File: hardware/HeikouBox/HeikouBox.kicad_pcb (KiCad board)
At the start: 2 copper layers, 100 x 100 mm, 198 parts, among them J101 5V, J201 Conn_02x05_Odd_Even, J202 Conn_02x08_Odd_Even, J301 DB15_Female_HighDensity_Mount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, J302 AudioJack3_SwitchTR, J501 Micro_SD_Card_TFP09-2-12B, J503 PS/2, Q301 MMBT3904, Q302 MMBT3904, Q303 MMBT3904, Q304 MMBT3904, Q305 MMBT3904, Q306 MMBT3904, Q307 MMBT3904, Q502 BSS138, Q503 BSS138, SW501 Left, SW502 Right, SW503 Up, SW504 Down, U101 LD1117S33TR, U102 LD1117S25TR, U103 LD1117S12TR, U201 HeikouBox-Core, U202 74HCU04, U401 K4S281632-UC60, U501 STM32-BluePill-Socket, Y201 14.31818MHz, Y202 28.37516MHz

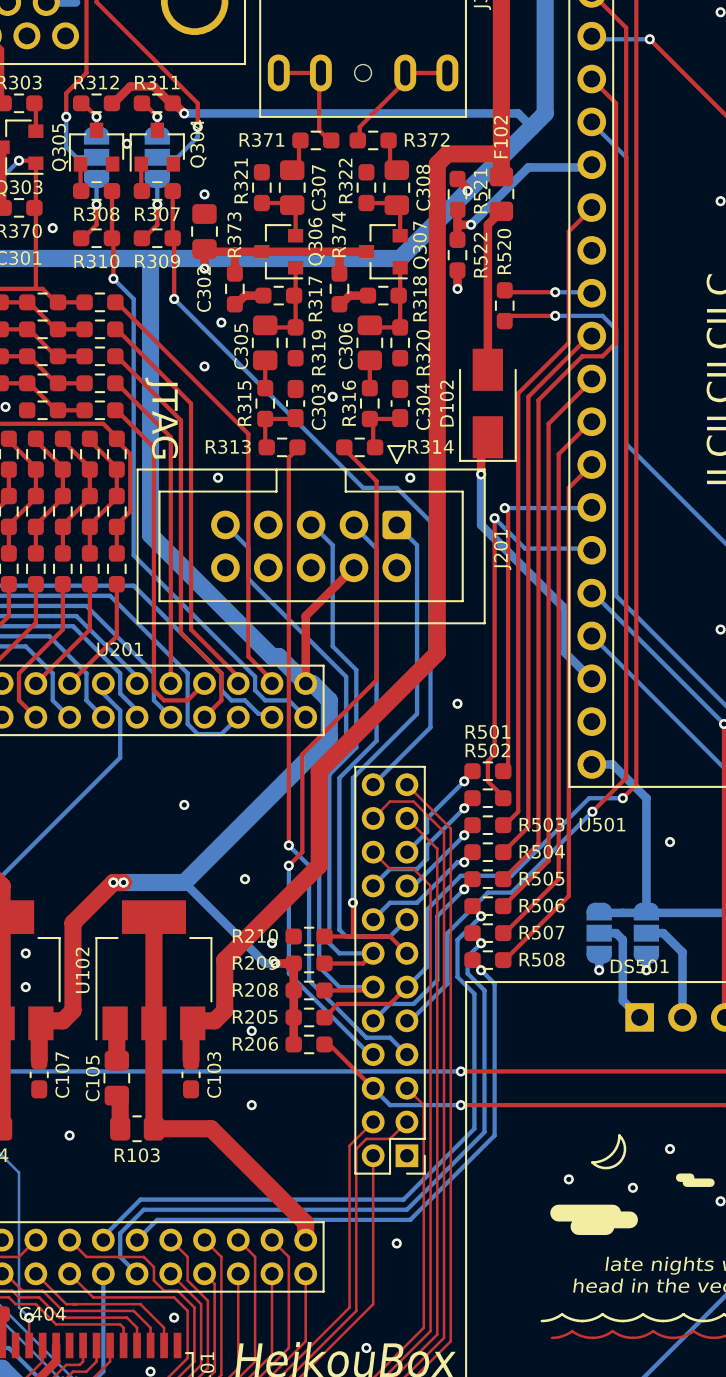
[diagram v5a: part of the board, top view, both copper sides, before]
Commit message: Connect UART correctly, remove unused mdb connection & mdb terminology
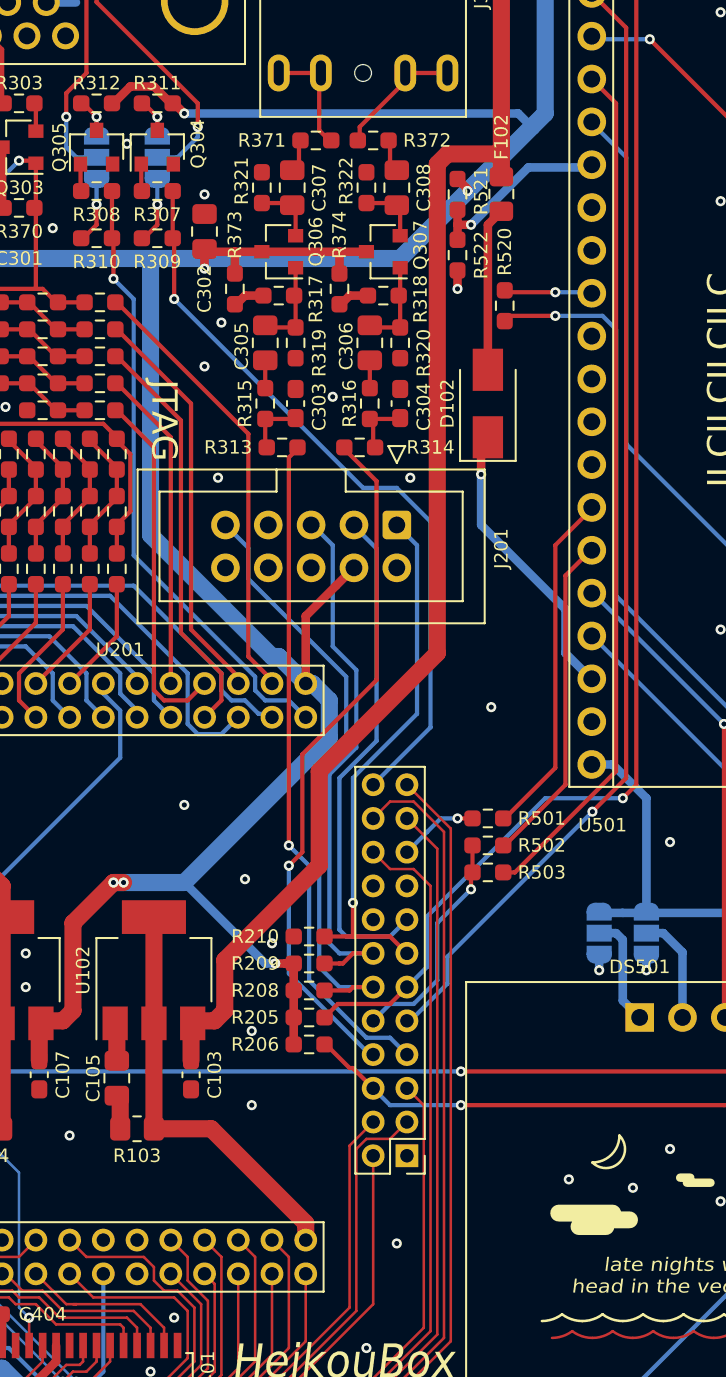
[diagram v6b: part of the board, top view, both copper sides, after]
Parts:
- removed R504, R505, R506, R507, R508: 1K, Resistor_SMD:R_0603_1608Metric_Pad0.98x0.95mm_HandSolder
- R313, R314: value 1K -> 2K2
- R315, R316: value 10K -> 1K
- moved R503 2.80 mm to (68.0, 77.4)
- moved R501 2.80 mm to (68.0, 74.2)
- moved R502 2.80 mm to (68.0, 75.8)
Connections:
- net /part2-core/mdb0 renamed /part2-core/dbg_RX
- net /part5-hub/MDB0_RX_R renamed /part5-hub/DBG_TX_R
- net /part5-hub/MDB1_TX_R renamed /part5-hub/DBG_RX_R
- D504 pad 2: Net-(D504-Pad2) -> (no net)
- J201 pad 6: Net-(J201-Pad6) -> (no net)
- J201 pad 7: Net-(J201-Pad7) -> (no net)
- J201 pad 8: Net-(J201-Pad8) -> (no net)
- J301 pad 11: Net-(J301-Pad11) -> (no net)
- J301 pad 12: Net-(J301-Pad12) -> (no net)
- J301 pad 15: Net-(J301-Pad15) -> (no net)
- J301 pad 4: Net-(J301-Pad4) -> (no net)
- J301 pad 5: Net-(J301-Pad5) -> (no net)
- J301 pad 9: Net-(J301-Pad9) -> (no net)
- J501 pad 1: Net-(J501-Pad1) -> (no net)
- J501 pad 8: Net-(J501-Pad8) -> (no net)
- J503 pad 2: Net-(J503-Pad2) -> (no net)
- J503 pad 6: Net-(J503-Pad6) -> (no net)
- R502 pad 2: /part2-core/mdb1 -> /part5-hub/cfg_DATA_dbg_RX
- R503 pad 1: /part5-hub/MDB2_R -> /part5-hub/CFG_DATA_R
- R503 pad 2: /part2-core/mdb2 -> /part5-hub/cfg_DATA_dbg_RX
- U201 pad 10: /part2-core/mdb4 -> /part5-hub/cfg_DATA_dbg_RX
- U201 pad 16: /part2-core/mdb3 -> (no net)
- U201 pad 17: /part2-core/mdb2 -> (no net)
- U201 pad 18: /part2-core/mdb1 -> (no net)
- U201 pad 83: /part2-core/mdb7 -> (no net)
- U201 pad 84: /part2-core/mdb6 -> (no net)
- U201 pad 85: /part2-core/mdb5 -> (no net)
- U202 pad 6: Net-(U202-Pad6) -> (no net)
- U202 pad 8: Net-(U202-Pad8) -> (no net)
- U401 pad 36: Net-(U401-Pad36) -> (no net)
- U401 pad 40: Net-(U401-Pad40) -> (no net)
- U501 pad 1: Net-(U501-Pad1) -> (no net)
- U501 pad 17: Net-(U501-Pad17) -> (no net)
- U501 pad 18: Net-(U501-Pad18) -> (no net)
- U501 pad 2: Net-(U501-Pad2) -> (no net)
- U501 pad 24: /part5-hub/MDB4_CD_R -> /part5-hub/CFG_DATA_R
- U501 pad 27: /part5-hub/MDB2_R -> (no net)
- U501 pad 28: Net-(U501-Pad28) -> (no net)
- U501 pad 3: Net-(U501-Pad3) -> (no net)
- U501 pad 30: /part5-hub/MDB3_R -> (no net)
- U501 pad 31: /part5-hub/MDB5_R -> (no net)
- U501 pad 32: /part5-hub/MDB6_R -> (no net)
- U501 pad 33: /part5-hub/MDB7_R -> (no net)
- U501 pad 4: Net-(U501-Pad4) -> (no net)
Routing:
- net /part5-hub/MDB4_CD_R: track 51.5 -> 0.00 mm
- net /part5-hub/CFG_DATA_R: track 0.00 -> 50.8 mm
- net /part2-core/mdb6: track 39.7 -> 0.00 mm, vias 1 -> 0
- net /part2-core/mdb5: track 39.3 -> 0.00 mm, vias 1 -> 0
- net /part5-hub/MDB2_R: track 38.8 -> 0.00 mm
- net /part2-core/mdb7: track 34.7 -> 0.00 mm, vias 1 -> 0
- net /part5-hub/MDB5_R: track 33.4 -> 0.00 mm
- net /part5-hub/MDB3_R: track 32.9 -> 0.00 mm
- net /part5-hub/MDB6_R: track 32.6 -> 0.00 mm
- net /part5-hub/MDB7_R: track 31.6 -> 0.00 mm
- net /part5-hub/cfg_DATA_dbg_RX: track 0.00 -> 13.7 mm, vias 0 -> 1
- net /part2-core/mdb4: track 11.7 -> 0.00 mm, vias 1 -> 0
- net /part2-core/mdb1: track 8.58 -> 0.00 mm, vias 1 -> 0
- net /part2-core/mdb3: track 7.61 -> 0.00 mm, vias 1 -> 0
- net /part2-core/mdb2: track 5.44 -> 0.00 mm, vias 1 -> 0
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
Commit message: Tidy PCB a bit
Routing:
- net /part2-core/jtag_TDO: track 30.0 -> 27.5 mm
- net /part2-core/cfg_NCFG: track 76.5 -> 74.8 mm
- net /part2-core/jtag_TDI: track 36.5 -> 35.3 mm
- net /part2-core/jtag_TMS: track 32.6 -> 31.4 mm
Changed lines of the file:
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@@
     (thickness 1.6)
     (drawings 74)
-    (tracks 1627)
+    (tracks 1621)
     (zones 0)
     (modules 193)
@@
     (add_net /part2-core/jtag_TDO)
     (add_net /part2-core/jtag_TMS)
-    (add_net /part2-core/mdb1)
-    (add_net /part2-core/mdb2)
-    (add_net /part2-core/mdb3)
-    (add_net /part2-core/mdb5)
-    (add_net /part2-core/mdb6)
-    (add_net /part2-core/mdb7)
     (add_net /part2-core/xbus0)
     (add_net /part2-core/xbus1)
@@
   (module KSK_HeikouBox:STM32-BluePill-Socket (layer F.Cu)
     (at 89.4 71 180)
-    (fp_text reference U501 (at 14.6 -3.6 180) (layer F.SilkS)
+    (fp_text reference U501 (at 0 -3.6 180) (layer F.SilkS)
       (effects (font (size 0.8 0.8) (thickness 0.127)))
     )
@@
   (segment (start 33.2 72.2) (end 39.2 78.2) (width 1.016) (layer F.Cu) (net 4))
   (segment (start 31.2 72.2) (end 33.2 72.2) (width 1.016) (layer F.Cu) (net 4))
-  (via (at 60 79.2) (size 0.6) (drill 0.3) (layers F.Cu B.Cu) (net 5))
-  (segment (start 60 79.2) (end 60 81.2) (width 0.254) (layer F.Cu) (net 5))
   (segment (start 60 81.2) (end 58.3125 81.2) (width 0.254) (layer F.Cu) (net 5))
   (segment (start 62.2 81.2) (end 60 81.2) (width 0.254) (layer F.Cu) (net 5))
   (segment (start 63.2 82.2) (end 62.2 81.2) (width 0.254) (layer F.Cu) (net 5))
-  (segment (start 60 71.8) (end 60 79.2) (width 0.254) (layer B.Cu) (net 5))
-  (segment (start 63.8 68) (end 60 71.8) (width 0.254) (layer B.Cu) (net 5))
-  (segment (start 63.8 58) (end 63.8 68) (width 0.254) (layer B.Cu) (net 5))
-  (segment (start 62.6 56.8) (end 63.8 58) (width 0.254) (layer B.Cu) (net 5))
-  (segment (start 62.2 81.2) (end 63.2 80.2) (width 0.254) (layer B.Cu) (net 6))
-  (segment (start 59.2 71.8) (end 59.2 80.8) (width 0.254) (layer B.Cu) (net 6))
-  (segment (start 61.4 58.2) (end 61.4 69.6) (width 0.254) (layer B.Cu) (net 6))
-  (segment (start 59.6 81.2) (end 62.2 81.2) (width 0.254) (layer B.Cu) (net 6))
+  (segment (start 63.8 58) (end 62.6 56.8) (width 0.254) (layer B.Cu) (net 5))
+  (segment (start 60 71.8) (end 63.8 68) (width 0.254) (layer B.Cu) (net 5))
+  (segment (start 60 77.2) (end 60 71.8) (width 0.254) (layer B.Cu) (net 5))
+  (segment (start 60 77.2) (end 60 81.2) (width 0.254) (layer F.Cu) (net 5))
+  (segment (start 63.8 68) (end 63.8 58) (width 0.254) (layer B.Cu) (net 5))
+  (via (at 60 77.2) (size 0.6) (drill 0.3) (layers F.Cu B.Cu) (net 5))
+  (segment (start 62.2 79.2) (end 63.2 80.2) (width 0.254) (layer B.Cu) (net 6))
+  (segment (start 60.6 79.2) (end 62.2 79.2) (width 0.254) (layer B.Cu) (net 6))
+  (segment (start 59.2 77.8) (end 60.6 79.2) (width 0.254) (layer B.Cu) (net 6))
   (segment (start 61.4 69.6) (end 59.2 71.8) (width 0.254) (layer B.Cu) (net 6))
+  (segment (start 59.2 71.8) (end 59.2 77.8) (width 0.254) (layer B.Cu) (net 6))
+  (segment (start 61.4 58.2) (end 61.4 69.6) (width 0.254) (layer B.Cu) (net 6))
   (segment (start 60.06 56.86) (end 61.4 58.2) (width 0.254) (layer B.Cu) (net 6))
-  (segment (start 59.2 80.8) (end 59.6 81.2) (width 0.254) (layer B.Cu) (net 6))
   (segment (start 60.06 56.8) (end 60.06 56.86) (width 0.254) (layer B.Cu) (net 6))
-  (segment (start 58.6 81.6) (end 59.2 82.2) (width 0.254) (layer B.Cu) (net 7))
   (segment (start 60.2 70) (end 58.6 71.6) (width 0.254) (layer B.Cu) (net 7))
   (segment (start 60.2 65.4) (end 60.2 70) (width 0.254) (layer B.Cu) (net 7))
-  (segment (start 58.6 71.6) (end 58.6 81.6) (width 0.254) (layer B.Cu) (net 7))
   (segment (start 58.8 64) (end 60.2 65.4) (width 0.254) (layer B.Cu) (net 7))
-  (segment (start 59.2 82.2) (end 61.2 82.2) (width 0.254) (layer B.Cu) (net 7))
   (segment (start 58.8 58) (end 58.8 64) (width 0.254) (layer B.Cu) (net 7))
   (segment (start 57.6 56.8) (end 58.8 58) (width 0.254) (layer B.Cu) (net 7))
@@
   (segment (start 59.4 82.8) (end 59.2 82.8) (width 0.254) (layer F.Cu) (net 7))
   (segment (start 60 82.2) (end 59.4 82.8) (width 0.254) (layer F.Cu) (net 7))
-  (segment (start 59.2 84.2) (end 61.2 84.2) (width 0.254) (layer B.Cu) (net 8))
+  (segment (start 61.2 82.2) (end 58.6 79.6) (width 0.254) (layer B.Cu) (net 7))
+  (segment (start 58.6 71.6) (end 58.6 79.6) (width 0.254) (layer B.Cu) (net 7))
   (segment (start 59.6 69.8) (end 58 71.4) (width 0.254) (layer B.Cu) (net 8))
-  (segment (start 58 71.4) (end 58 83) (width 0.254) (layer B.Cu) (net 8))
   (segment (start 59.6 65.8) (end 59.6 69.8) (width 0.254) (layer B.Cu) (net 8))
-  (segment (start 58 83) (end 59.2 84.2) (width 0.254) (layer B.Cu) (net 8))
   (segment (start 53.8 60) (end 59.6 65.8) (width 0.254) (layer B.Cu) (net 8))
   (segment (start 53.8 58.16) (end 53.8 60) (width 0.254) (layer B.Cu) (net 8))
@@
   (segment (start 61.2 84.2) (end 60 84.2) (width 0.254) (layer F.Cu) (net 8))
   (segment (start 58.3125 84.4) (end 59.8 84.4) (width 0.254) (layer F.Cu) (net 8))
+  (segment (start 61.2 84.2) (end 58 81) (width 0.254) (layer B.Cu) (net 8))
+  (segment (start 58 71.4) (end 58 81) (width 0.254) (layer B.Cu) (net 8))
   (segment (start 24.4 83.2) (end 22 80.8) (width 0.254) (layer B.Cu) (net 9))
   (segment (start 30.2 83.2) (end 24.4 83.2) (width 0.254) (layer B.Cu) (net 9))
@@
   (segment (start 55 68) (end 54.4 68) (width 0.254) (layer B.Cu) (net 24))
   (segment (start 55.2 68.2) (end 55 68) (width 0.254) (layer B.Cu) (net 24))
-  (via (at 74.2 73.8) (size 0.6) (drill 0.3) (layers F.Cu B.Cu) (net 25))
+  (segment (start 66.4 83) (end 63.2 86.2) (width 0.254) (layer B.Cu) (net 25))
+  (via (at 66.4 83) (size 0.6) (drill 0.3) (layers F.Cu B.Cu) (net 25))
   (segment (start 76.2 27.32) (end 74.16 25.28) (width 0.254) (layer F.Cu) (net 25))
   (segment (start 76.2 71.8) (end 76.2 27.32) (width 0.254) (layer F.Cu) (net 25))
-  (segment (start 74.2 73.8) (end 76.2 71.8) (width 0.254) (layer F.Cu) (net 25))
-  (segment (start 63.4 86.2) (end 63.2 86.2) (width 0.254) (layer B.Cu) (net 25))
-  (segment (start 65.6 84) (end 63.4 86.2) (width 0.254) (layer B.Cu) (net 25))
-  (segment (start 65.6 82.4) (end 65.6 84) (width 0.254) (layer B.Cu) (net 25))
-  (segment (start 74.2 73.8) (end 65.6 82.4) (width 0.254) (layer B.Cu) (net 25))
+  (segment (start 66.4 81.6) (end 76.2 71.8) (width 0.254) (layer F.Cu) (net 25))
+  (segment (start 66.4 83) (end 66.4 81.6) (width 0.254) (layer F.Cu) (net 25))
   (segment (start 59.1125 85.2) (end 58.3125 86) (width 0.254) (layer F.Cu) (net 26))
   (segment (start 62.2 85.2) (end 59.1125 85.2) (width 0.254) (layer F.Cu) (net 26))
   (segment (start 63.2 84.2) (end 62.2 85.2) (width 0.254) (layer F.Cu) (net 26))
-  (via (at 76 73) (size 0.6) (drill 0.3) (layers F.Cu B.Cu) (net 26))
   (segment (start 74.16 22.76) (end 74.16 22.74) (width 0.254) (layer F.Cu) (net 26))
   (segment (start 76.8 25.4) (end 74.16 22.76) (width 0.254) (layer F.Cu) (net 26))
   (segment (start 76.8 72.2) (end 76.8 25.4) (width 0.254) (layer F.Cu) (net 26))
-  (segment (start 76 73) (end 76.8 72.2) (width 0.254) (layer F.Cu) (net 26))
-  (segment (start 64.4 83) (end 63.2 84.2) (width 0.254) (layer B.Cu) (net 26))
-  (segment (start 64.4 80) (end 64.4 83) (width 0.254) (layer B.Cu) (net 26))
-  (segment (start 71.4 73) (end 64.4 80) (width 0.254) (layer B.Cu) (net 26))
-  (segment (start 76 73) (end 71.4 73) (width 0.254) (layer B.Cu) (net 26))
+  (segment (start 67.2 81.8) (end 76.8 72.2) (width 0.254) (layer F.Cu) (net 26))
+  (via (at 67.2 81.8) (size 0.6) (drill 0.3) (layers F.Cu B.Cu) (net 26))
+  (segment (start 65.6 81.8) (end 63.2 84.2) (width 0.254) (layer B.Cu) (net 26))
+  (segment (start 67.2 81.8) (end 65.6 81.8) (width 0.254) (layer B.Cu) (net 26))
   (segment (start 58.3125 87.4875) (end 58.3125 87.6) (width 0.254) (layer F.Cu) (net 27))
   (segment (start 62.2 91.2) (end 61.2 90.2) (width 0.254) (layer B.Cu) (net 27))
@@
   (segment (start 69 74.2) (end 72 71.2) (width 0.254) (layer F.Cu) (net 182))
   (segment (start 68.9125 74.2) (end 69 74.2) (width 0.254) (layer F.Cu) (net 182))
-  (via (at 67 78.4) (size 0.6) (drill 0.3) (layers F.Cu B.Cu) (net 183))
-  (segment (start 62.2 85.2) (end 61.2 86.2) (width 0.254) (layer B.Cu) (net 183))
-  (segment (start 63.6 85.2) (end 62.2 85.2) (width 0.254) (layer B.Cu) (net 183))
-  (segment (start 65 83.8) (end 63.6 85.2) (width 0.254) (layer B.Cu) (net 183))
-  (segment (start 65 80.4) (end 65 83.8) (width 0.254) (layer B.Cu) (net 183))
-  (segment (start 67 78.4) (end 65 80.4) (width 0.254) (layer B.Cu) (net 183))
-  (segment (start 67 77.4875) (end 67.0875 77.4) (width 0.254) (layer F.Cu) (net 183))
-  (segment (start 67 78.4) (end 67 77.4875) (width 0.254) (layer F.Cu) (net 183))
   (segment (start 67.0875 77.4) (end 67.0875 75.8) (width 0.254) (layer F.Cu) (net 183))
+  (segment (start 67 77.4875) (end 67.0875 77.4) (width 0.254) (layer F.Cu) (net 183))
+  (via (at 67 78.2) (size 0.6) (drill 0.3) (layers F.Cu B.Cu) (net 183))
+  (segment (start 67 78.2) (end 67 77.4875) (width 0.254) (layer F.Cu) (net 183))
+  (segment (start 62.2 85.2) (end 61.2 86.2) (width 0.254) (layer B.Cu) (net 183))
+  (segment (start 62.2 81.8) (end 62.2 85.2) (width 0.254) (layer B.Cu) (net 183))
+  (segment (start 62.8 81.2) (end 62.2 81.8) (width 0.254) (layer B.Cu) (net 183))
+  (segment (start 64 81.2) (end 62.8 81.2) (width 0.254) (layer B.Cu) (net 183))
+  (segment (start 67 78.2) (end 64 81.2) (width 0.254) (layer B.Cu) (net 183))
   (segment (start 69 75.8) (end 68.9125 75.8) (width 0.254) (layer F.Cu) (net 184))
   (segment (start 72.6 72.2) (end 69 75.8) (width 0.254) (layer F.Cu) (net 184))

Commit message: Upload latest files
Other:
- net class Default removed
- net class Power removed
- net class Signal removed
